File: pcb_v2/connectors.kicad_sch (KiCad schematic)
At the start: 15 parts, among them J1 RJ45, J2 RJ45, J5 Screw_Terminal_01x03, U1 VL53L0CXV0DH1

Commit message: Replace schematic RJ45 with symbol from the library
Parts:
- removed J1, J2: RJ45, Connector_RJ:RJ45_Amphenol_54602-x08_Horizontal, symbol A-2004-2-4-LPS-N-R:A-2004-2-4-LPS-N-R
- added J7, J8: RJ45_Shielded, Connector_RJ:RJ45_Amphenol_54602-x08_Horizontal, symbol Connector:RJ45_Shielded
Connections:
- net DESK_1: now also J7.1, J8.1
- net DESK_2: now also J7.2, J8.2
- net DESK_4: now also J7.4, J8.4
- net DESK_6: now also J7.6, J8.6
- net DESK_7: now also J7.7, J8.7
- net DESK_8: now also J7.8, J8.8
- net GND: now also J7.3, J7.SH, J8.3, J8.SH
- net VDD: now also J7.5, J8.5

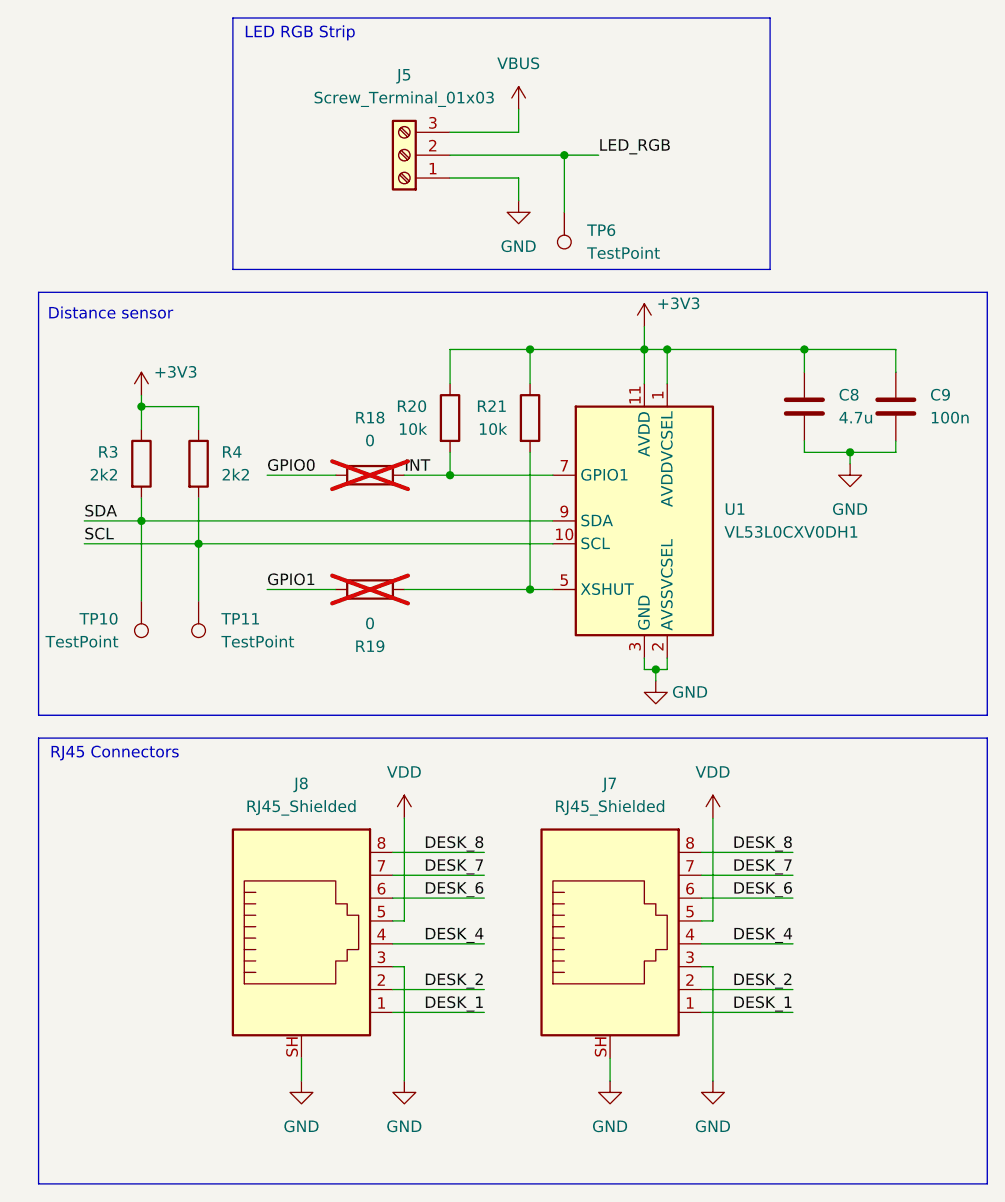
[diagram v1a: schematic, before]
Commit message: Connect pin sheets. Add protection on USB. Use SolderJumpers.
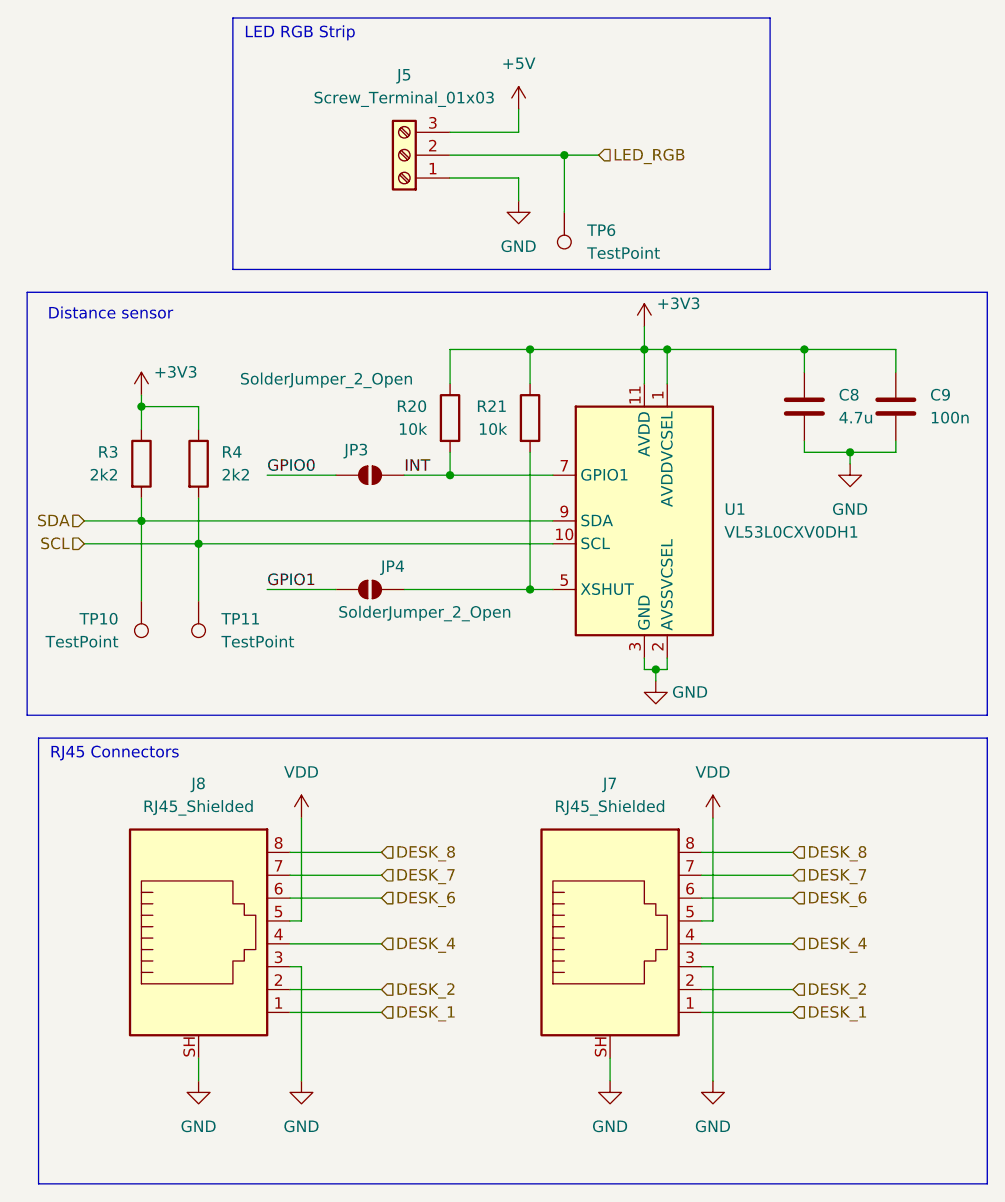
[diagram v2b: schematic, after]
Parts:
- removed R18, R19: 0, Resistor_SMD:R_0402_1005Metric, symbol Device:R
- added JP3, JP4: SolderJumper_2_Open, symbol Jumper:SolderJumper_2_Open
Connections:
- net GPIO0: now also JP3.1 (A)
- net GPIO1: now also JP4.1 (A)
- net INT: now also JP3.2 (B)
- net at R21.2, U1.5 (XSHUT): now also JP4.2 (B)
- net VBUS renamed +5V
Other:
- moved on the sheet: J8
